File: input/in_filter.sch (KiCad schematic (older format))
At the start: 17 parts

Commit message: Work on schematics for antialias_driver.sch and in_filter.sch.  Spice simulations of antialias filter and reference driver.
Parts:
- removed R?: 20, Resistor_SMD:R_0603_1608Metric, symbol Device:R_US
- added C? (x4): 1uF, Capacitor_SMD:C_0603_1608Metric, symbol Device:C_Small
- added R? (x5): 10, Resistor_SMD:R_0805_2012Metric, symbol Device:R_US
- R?: value 20 -> 10; footprint Resistor_SMD:R_0603_1608Metric -> Resistor_SMD:R_0805_2012Metric; Digikey (none) -> 541-10TACT-ND; MPN (none) -> CRCW080510R0JNEAHP; Notes (none) -> Thick film surge resist
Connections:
- wire segments 45 -> 55
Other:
- moved on the sheet: C?, D?A, D?B, R?

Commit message: Continuing work on input board, also added some design files and PDF documentation for the prototype source and sensor.  Deleted various spurious kicad project files.  The main project for the input board is now input_board.pro.
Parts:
- added D105, D106: BAV99, Package_TO_SOT_SMD:SOT-23, symbol Diode:BAV99
- added R123, R124: 10K 0.1%, Resistor_SMD:R_0603_1608Metric, symbol Device:R_US
- gave numbers to parts that had none: 23
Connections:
- net labels added: BIST++, BIST+-, BIST-+, BIST--, BIST_feedback
- wire segments 55 -> 73
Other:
- note added: "Built In Self Test is normally disconnected by driving the BIST?- lines to V+\nand the BIST?+ lines to V-. The reverse-biased diodes have low capacitance,\nabout 1.1 pF each. \n\nThe BIST?? lines are global, so all channels are driven at the same levels.\nThe feedback connection allows us to cancel the diode Vf when on, but \nthis is connected only on the first channel, so others only track as we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"
- moved on the sheet: C109, C110, C111, C112, C113, C114, C115, R110, R111, R112

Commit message: Mainly work on the top level of the input board, attaching signals to the channels, digital I/O.  Decided to use Eurocard 64 pin type B connector for the connection to the main board.  See input_board_pinout.txt.
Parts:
- removed C108: 1nF, Capacitor_SMD:C_0805_2012Metric, symbol Device:C_Small
- removed C110: 1uF, Capacitor_SMD:C_0603_1608Metric, symbol Device:C_Small
- removed unit 2 of D105
- removed unit 2 of D106
- added C121: 1nF, Capacitor_SMD:C_0805_2012Metric, symbol Device:C_Small
- added C123: 1uF, Capacitor_SMD:C_0603_1608Metric, symbol Device:C_Small
- added D107, D108: BAV99, Package_TO_SOT_SMD:SOT-23, symbol Diode:BAV99
- added R121, R122: 10K 0.1%, Resistor_SMD:R_0603_1608Metric, symbol Device:R_US
- renumbered C107 to C120, C109 to C122, C111 to C124, C112 to C125, C113 to C126, C114 to C127, C115 to C128, R106 to R115, R107 to R116, R108 to R117, R109 to R118, R110 to R119, R124 to R120, R111 to R124, R112 to R125
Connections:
- net labels added: +sense, -sense
- wire segments 73 -> 77
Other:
- note added: "Built In Self Test is normally disconnected by driving the BIST?- lines to V+\nand the BIST?+ lines to V-. The reverse-biased diodes have low capacitance,\nabout 1.1 pF each. Only one diode in each package is used because we need \nindependent access to both ends of the diode.\n\nThe BIST?? lines are global, so all channels are driven at the same levels.\nThe feedback connection allows us to canc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"
- note removed: "Built In Self Test is normally disconnected by driving the BIST?- lines to V+\nand the BIST?+ lines to V-. The reverse-biased diodes have low capacitance,\nabout 1.1 pF each. \n\nThe BIST?? lines are global, so all channels are driven at the same levels.\nThe feedback connection allows us to cancel the diode Vf when on, but \nthis is connected only on the first channel, so others only track as we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"
- moved on the sheet: D105A, D106A, R120

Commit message: Still beating into overall shape.  This is a checkpoint before modifying the analog signal chain to fold the diff amp and antialias into the driver, going to a full differential path.
Overall: Changes to component attributes to reduce duplicates in BOM, and added links to Digikey and datasheets.

board_connector.sch: Added reference input pins, decimation SEL lines.

in_filter.sch:
Fixed BIST feedback to be taken at the top of each injection resistor (4 lines, not 2)

input_board.sch:
Added some missing connections and no-connects.

power_budget.xlsx:
Much more elaborate now, models effect of input levels on load currents, computes currents and total power, for several variants.

reference_buffer.sch:
Updated with booster sink transistor to handle sourcing into reference by ADC clamp diodes.

simetrix/:
Added supply_negative.wxsch and supply_positive.wxsch, which are concepts for low noise lowish dropout regulators for the analog rails.  Other simetrix modifications are cosmetic.
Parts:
- added E1: 2036-07-SMLF, symbol ilemt_input:GDT
- C122: value 3.3 nF -> 3.3nF
- FB101, FB102: value 2K -> 600 Ohm
- R120, R121, R122, R123: value 10K 0.1% -> 10K; Notes (none) -> 0.1%
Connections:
- net labels added: sense++, sense+-, sense-+, sense--
- net labels removed: +sense, -sense
- wire segments 77 -> 80
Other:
- note added: "Input filter, transient/ESD protection and BIST injection"
- moved on the sheet: C120, C121, C122, C123, C124, C125, C126, C127, C128, D101, D102, D103A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

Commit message: Changes mostly related to avoiding excess power consumption.  This is mainly by limiting the signal swing to 0..5V and using asymmetric supplies of -4V and +8V.  (Perhaps we can reduce these to 3/7 V.)  Also, I got rid of two stages in the input signal path.
power_budget.xlsx
power.sch
reference_buffer.sch:
Changes related to the new supply voltages, and start on the power supply section.

input_channel.sch
in_amp.sch
antialias_driver.sch:
Reworked the input signal chain to keep a full differential path, rolling the antialias filter
into the ADC driver.  Also, related to change to lower asymmetrical supply voltages, there is
no 20V PP anywhere (the this was for benefit of the antialias filter noise, but that stage is gone).  Also, added zener clamp on VREF in driver.

in_filter.sch: added missing DC bias resistors.
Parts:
- added R113, R114, R131, R132: 200K, Resistor_SMD:R_0603_1608Metric, symbol Device:R_US
- D103, D104, D105, D106, D107, D108: value BAV99 -> BAS21S
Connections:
- net labels added: V+, V-, VREF
- net labels removed: +15V, -15V
- wire segments 80 -> 92
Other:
- note added: "Capacitance matching between + and - inputs is critical for \ncommon mode rejection. 1 nF capacitors are 1% C0G, and\ndiodes are chosen for low capacitance to minimize\nincidental capacitance mismatch."
- note added: "Placed at amp input, on \nper-channel analog ground\n===>>"
- note added: "Placed at connector\non chassis ground\n<<==="
- note removed: "Capacitance matching between + and - inputs is critical for \ncommon mode rejection. 1 nF capacitors are 1% C0G"
- note removed: "Placed at amp input, on per-channel analog ground"
- note removed: "Placed at connector on chassis ground"
- moved on the sheet: C120, C121, C122, C123, C124, C125, C126, C127, C128, D101, D102, D103A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

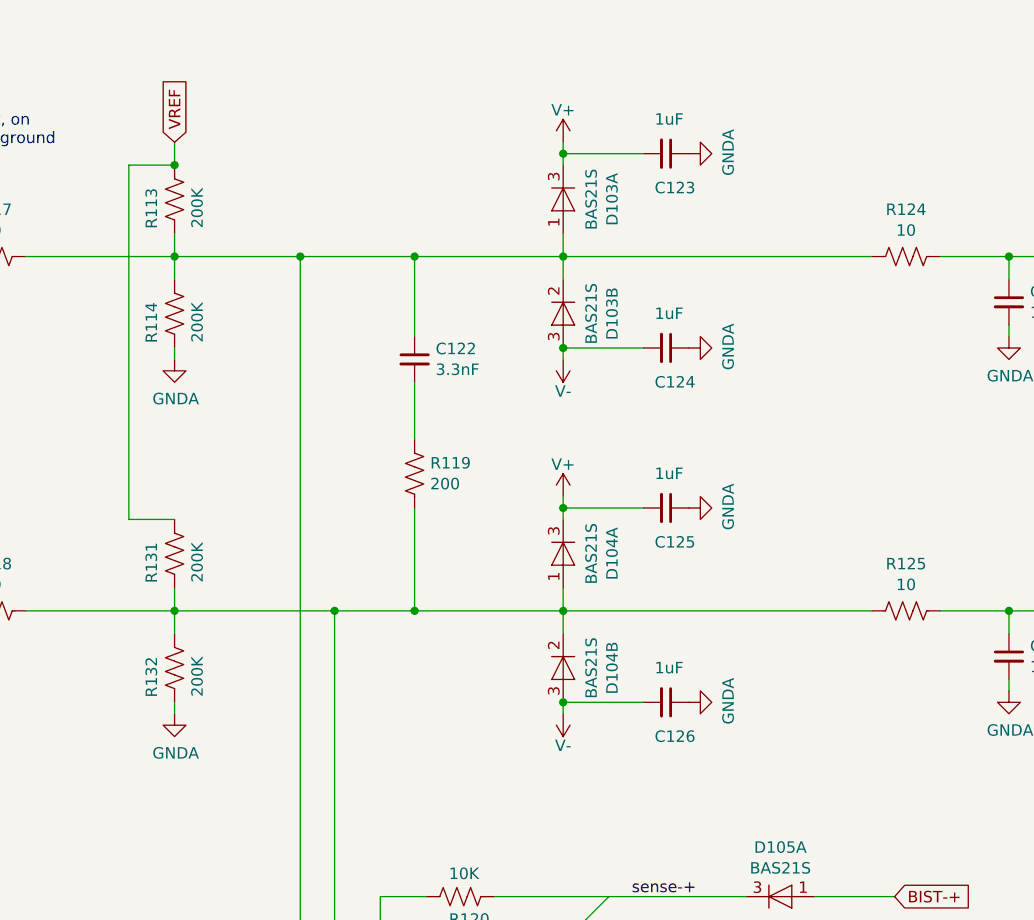
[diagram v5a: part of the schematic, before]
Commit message: Mostly work on power, regulators and distribution.  Also more BOM cleanup.
All of the bypass capacitors are now spec'd and in the DigiKey BOM. TVS zeners are now
spec'd.  Folded together some resistor values and got rid of some 1206 parts that no longer
need that much power rating at the lower supplies.

A affecting all of the input channel sheets is that we now distribute filtered V+, V- and VREF
via sheet ports.  The V+, V- filter is on input_channel.sch and the VREF filter is still in
adc.sch, but is distributed out to the other sheets that need it.

bist_buffer.sch: added buffer for built-in self-test

board_connector.sch: put the input filter for the analog supplies here.

power.sch: added regulators for the supplies.

reference_buffer.sch:
changed components to match those chosen for the V+, V- regulators and added
current steering diodes to bootstrap the reference buffer supply.  This is
necessary because the analog supplies are now derived from VREF.

*.wxsch:
Updates to spice models related to work on supplies.
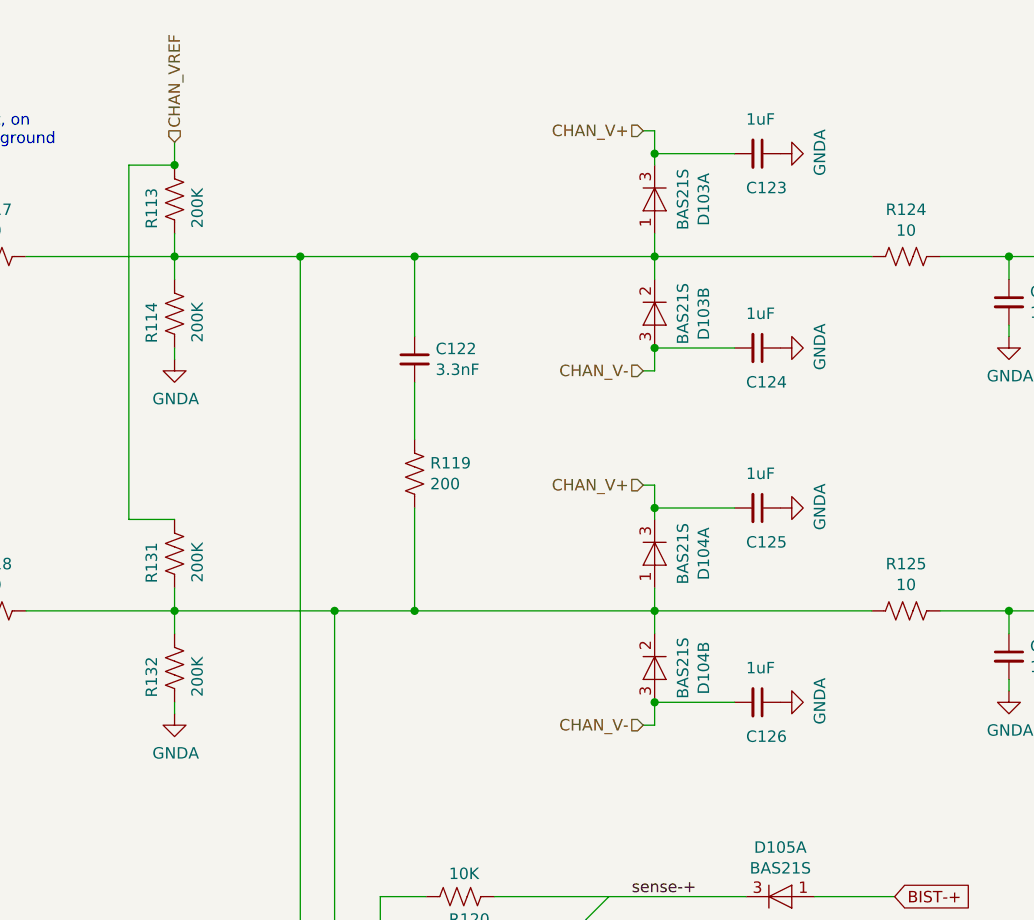
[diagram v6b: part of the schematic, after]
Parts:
- C123, C124, C125, C126: footprint Capacitor_SMD:C_0603_1608Metric -> Capacitor_SMD:C_0805_2012Metric; Description (none) -> CAP CER 1UF 16V X7R 0805; Digikey (none) -> 1276-6471-1-ND; MPN (none) -> CL21B105KOFNNNG
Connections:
- net V+ renamed CHAN_V+
- net V- renamed CHAN_V-
- net VREF renamed CHAN_VREF
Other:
- moved on the sheet: C123, C124, C125, C126, D103A, D103B, D104A, D104B

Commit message: Cleanup to get ready to start board layout. I had to get rid off all the bus signals, since in Kicad busses don't work that way.  Added a couple testpoints; many more needed.
Work on component placement in PCB.  I changed DGND to plain GND and "protective earth" to
"earth" (for chassis ground).  Chassis ground is now connected on the board only via a capacitor.
I had to fix the connector footprint to match the pin numbers on the symbol (there was a case
difference).
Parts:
- D103, D104, D105, D106, D107, D108: symbol Diode:BAV99 -> ilemt_input:BAS21S
- E1: footprint (none) -> input:GDT_3LINE_Bourns_2036-xx-SM
- FB101, FB102: footprint digikey-footprints:0805 -> Inductor_SMD:L_0805_2012Metric
- FL101: footprint (none) -> input:L_CommonMode_Bourns_DR331; symbol Device:EMI_Filter_LL_1423 -> ilemt_input:my_EMI_Filter_LL
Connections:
- net CHAN_V+: now also D103.2 (K), D104.2 (K); no longer D103.3 (K), D104.3 (K)
- net CHAN_V-: now also D103.1 (A), D104.1 (A); no longer D103.3 (A), D104.3 (A)
- net at C120.1, FB101.2: now also FL101.1; no longer FL101.2
- net at C121.1, FB102.2: now also FL101.2; no longer FL101.1
- net at C122.1, R113.1, R114.2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: now also D103.3 (A), D103.3 (K); no longer D103.1 (A), D103.2 (K)
- net at R118.1, R119.2, R120.2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: now also D104.3 (A), D104.3 (K); no longer D104.1 (A), D104.2 (K)
- net at D101.1 (A1), R115.2: now also FL101.4; no longer FL101.3
- net at D102.1 (A1), R116.2: now also FL101.3; no longer FL101.4
- net Earth_Protective renamed Earth
- net sense++ renamed BIST++_FB
- net sense+- renamed BIST+-_FB
- net sense-+ renamed BIST-+_FB
- net sense-- renamed BIST--_FB
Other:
- moved on the sheet: C120, C121, D101, D102, D105A, D106A, D107B, D108B, R120, R121, R122, R123
